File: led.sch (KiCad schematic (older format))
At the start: 4 parts

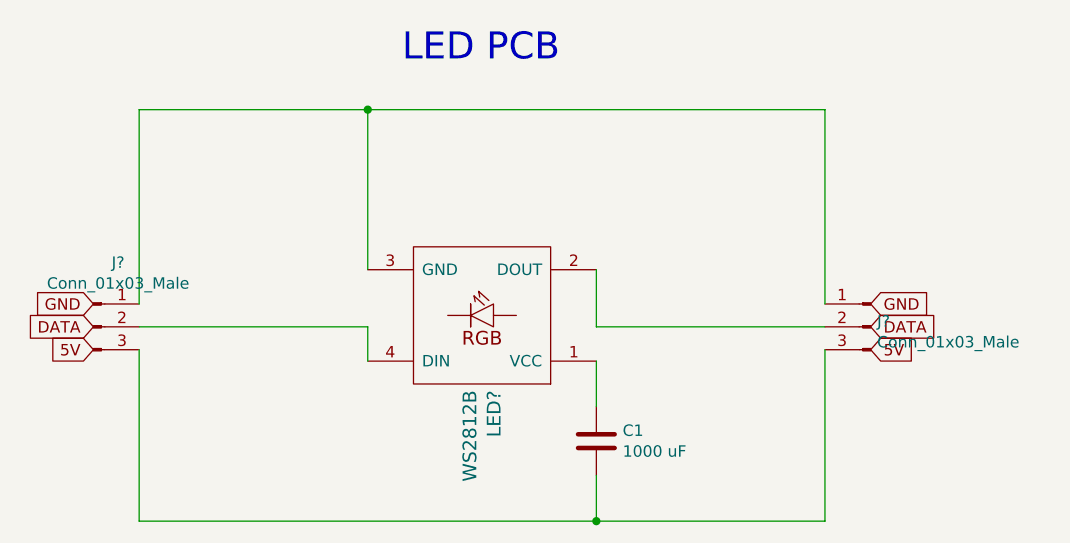
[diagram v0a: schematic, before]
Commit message: updated led schematic
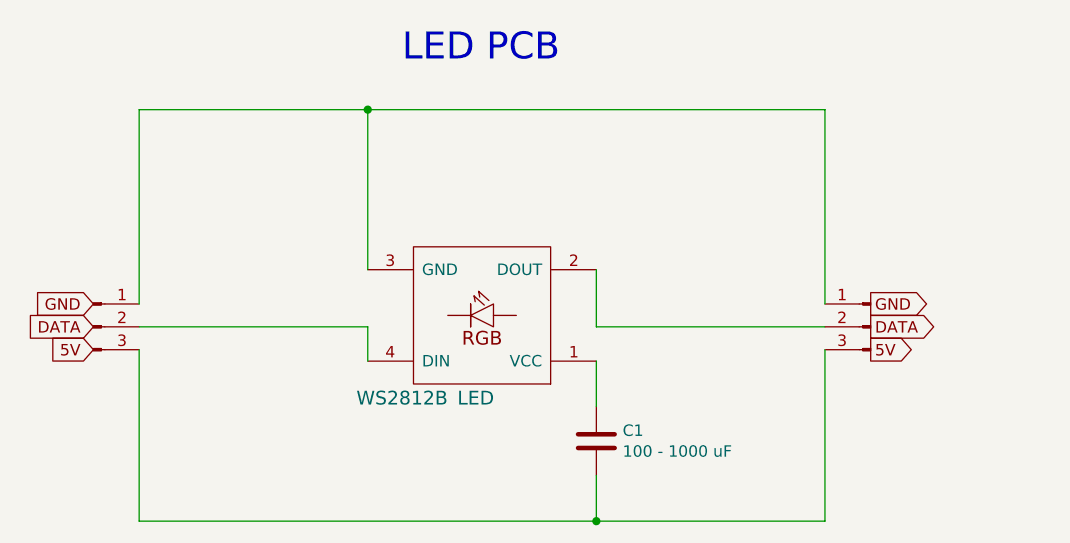
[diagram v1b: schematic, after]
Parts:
- C1: value 1000 uF -> 100 - 1000 uF
- gave numbers to parts that had none: 1
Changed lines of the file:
@@
 U 1 1 607A4CB2
 P 1300 2050
-F 0 "J?" H 1408 2331 50  0000 C CNN
-F 1 "Conn_01x03_Male" H 1408 2240 50  0000 C CNN
+F 0 "J?" H 1408 2331 50  0001 C CNN
+F 1 "Conn_01x03_Male" H 1408 2240 50  0001 C CNN
 F 2 "" H 1300 2050 50  0001 C CNN
 F 3 "~" H 1300 2050 50  0001 C CNN
@@
 U 1 1 607A2A3A
 P 4700 2050
-F 0 "J?" H 4672 2074 50  0000 R CNN
-F 1 "Conn_01x03_Male" H 4672 1983 50  0000 R CNN
+F 0 "J?" H 4672 2074 50  0001 R CNN
+F 1 "Conn_01x03_Male" H 4672 1983 50  0001 R CNN
 F 2 "" H 4700 2050 50  0001 C CNN
 F 3 "~" H 4700 2050 50  0001 C CNN
@@
 Text GLabel 1300 2050 0    50   Input ~ 0
 DATA
-Text GLabel 4700 1950 2    50   Input ~ 0
-GND
-Text GLabel 4700 2050 2    50   Input ~ 0
+Text GLabel 4700 2050 2    50   Output ~ 0
 DATA
-Text GLabel 4700 2150 2    50   Input ~ 0
+Text GLabel 4700 2150 2    50   Output ~ 0
 5V
 Text GLabel 1300 2150 0    50   Input ~ 0
@@
 	3500 1800 3500 2050
 $Comp
-L ws2812b:WS2812B LED?
+L ws2812b:WS2812B LED
 U 1 1 6079C2AE
 P 3000 2000
-F 0 "LED?" V 2947 2328 60  0000 L CNN
-F 1 "WS2812B" V 3053 2328 60  0000 L CNN
+F 0 "LED" H 2947 2362 60  0000 L CNN
+F 1 "WS2812B" H 3150 2362 60  0000 L CNN
 F 2 "" V 2950 2000 60  0000 C CNN
 F 3 "" V 2950 2000 60  0000 C CNN
@@
 P 3500 2550
 F 0 "C1" H 3615 2596 50  0000 L CNN
-F 1 "1000 uF" H 3615 2505 50  0000 L CNN
+F 1 "100 - 1000 uF" H 3615 2505 50  0000 L CNN
 F 2 "" H 3538 2400 50  0001 C CNN
 F 3 "~" H 3500 2550 50  0001 C CNN
@@
 Text Notes 2650 900  0    118  ~ 0
 LED PCB
+Text GLabel 4700 1950 2    50   Output ~ 0
+GND
 $EndSCHEMATC
